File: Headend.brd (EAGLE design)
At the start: 65.4 x 48.6 mm, 56 parts, among them IC1 317EMP, Q1 12.288Mhz, SW1 SPST_TACT-KMR2, U1 TXS0102

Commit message: Update board design
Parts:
- moved R8 29.3 mm to (14.8, 17.8), turned to 180 degrees
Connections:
- removed net N$12: COMMS_CPU.GPIO15, R8.1
- removed net N$6: COMMS_CPU.RESET, R9.1, SW1.1, SW1.3
- new net TEENSYCS: COMMS_CPU.GPIO15, R8.2, UI_CPU.10
- new net WATCHDOG: COMMS_CPU.RESET, R9.1, SW1.1, SW1.3, UI_CPU.2
- net +3V3: no longer R8.2
- net GND: now also R8.1
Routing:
- net TEENSYCS: track 0.00 -> 46.7 mm
- net WATCHDOG: track 0.00 -> 39.3 mm
- net N$6: track 19.2 -> 0.00 mm
- net GND: track 55.6 -> 46.7 mm
- net XDCS: track 36.5 -> 45.0 mm
- net N$12: track 5.25 -> 0.00 mm
- net +3V3: track 172.4 -> 171.3 mm

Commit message: Update board with further tweaks
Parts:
- removed SW1: SPST_TACT-KMR2, adafruit:KMR2
- added C22, C23: 10uF, adafruit:C0402
- added PGM_SW: SPST_TACT-KMR2, adafruit:KMR2
- C1, C2: value 8uF -> 10uF
- C13, C14: value 33pF -> 10pF
- moved RESET_SW 37.3 mm to (17.8, 40.6), turned to 180 degrees
- moved R13 0.95 mm to (62.6, 17.4), turned to 315 degrees
- moved C7 0.32 mm to (51.7, 15.9)
- moved C10 0.32 mm to (49.6, 21.9)
- turned C6 to 315 degrees
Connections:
- net +3V3: now also C22.1, C23.1
- net GND: now also C22.2, C23.2, PGM_SW.2, PGM_SW.4; no longer SW1.2, SW1.4
- net WATCHDOG: now also RESET_SW.1, RESET_SW.3; no longer SW1.1, SW1.3
- net XDCS: now also PGM_SW.1, PGM_SW.3; no longer RESET_SW.1, RESET_SW.3
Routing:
- net GND: track 46.7 -> 28.7 mm
- net N$19: track 6.13 -> 4.63 mm

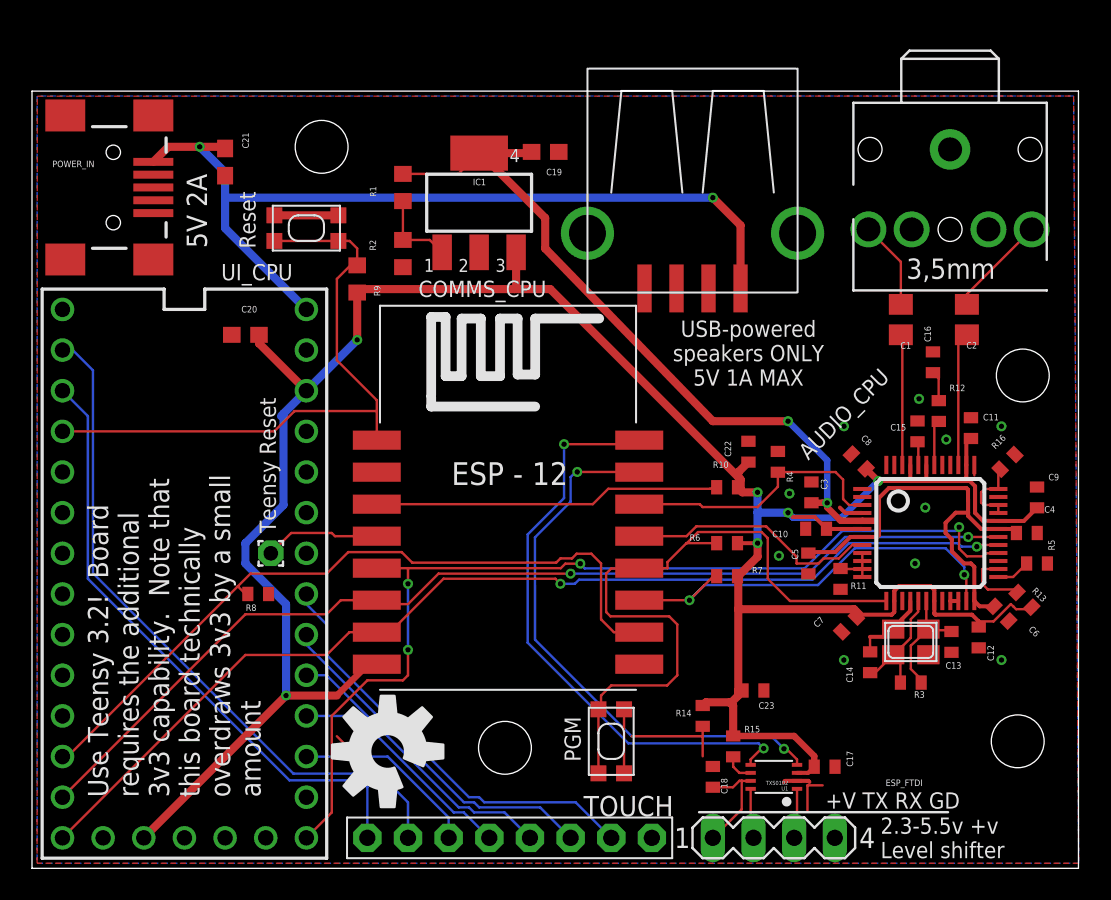
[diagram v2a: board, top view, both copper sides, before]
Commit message: Update design, clean up spurious resistor between 3v3 and Gnd, clean up some routing
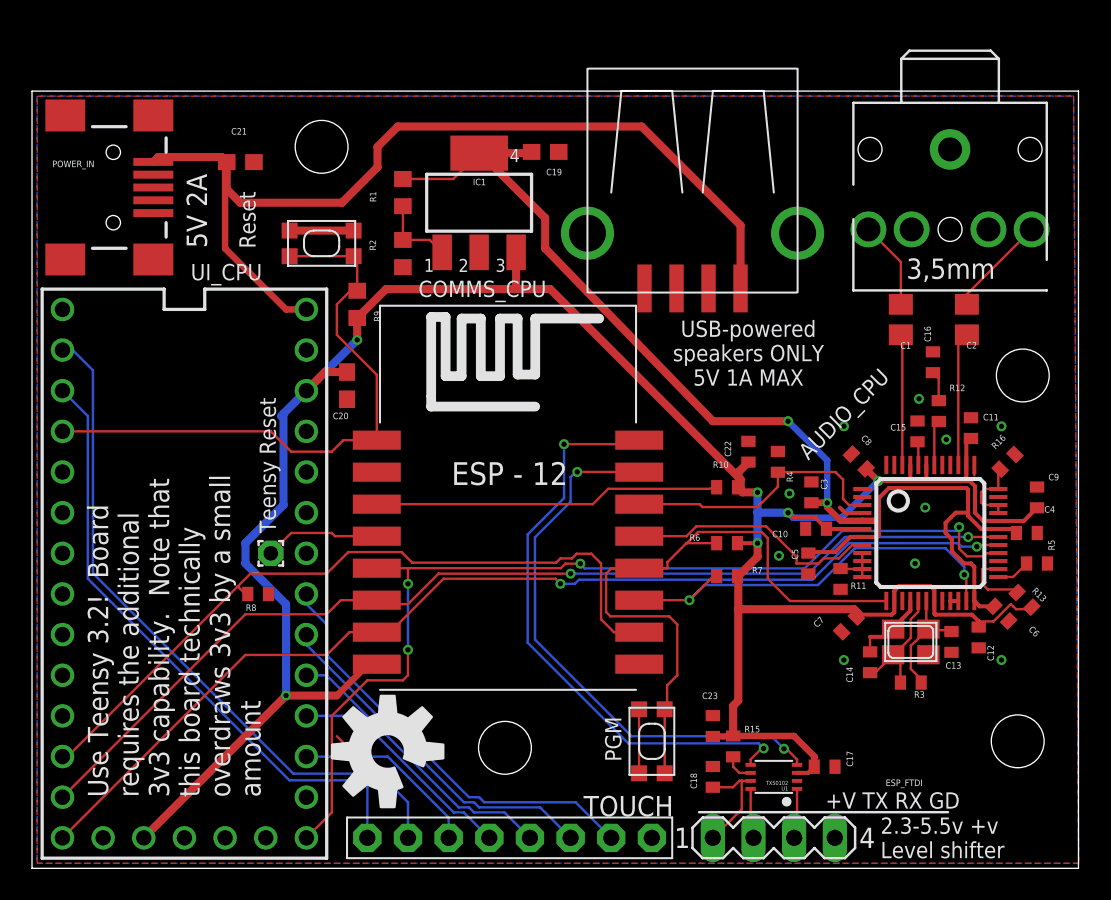
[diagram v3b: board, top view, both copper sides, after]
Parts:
- removed R14: 10k, adafruit:R0402
- moved C20 7.10 mm to (20.3, 30.8), turned to 270 degrees
- moved C23 3.38 mm to (43.2, 9.53), turned to 90 degrees
- moved PGM_SW 2.54 mm to (39.4, 8.57), turned to 270 degrees
- moved R9 1.59 mm to (21.0, 35.9)
- moved RESET_SW 1.35 mm to (18.7, 39.7)
- moved C21 0.95 mm to (13.7, 44.8), turned to 0 degrees
- moved R1 0.32 mm to (23.8, 42.9)
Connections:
- net +3V3: no longer R14.1
- net GND: no longer R14.2
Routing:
- net GND: track 28.7 -> 18.2 mm
- net +5V: track 54.7 -> 60.3 mm, vias 2 -> 0
- net XDCS: track 45.0 -> 41.2 mm
- net +3V3: track 170.9 -> 167.3 mm
- net WATCHDOG: track 39.3 -> 38.7 mm

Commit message: Updated with more reddit feedback
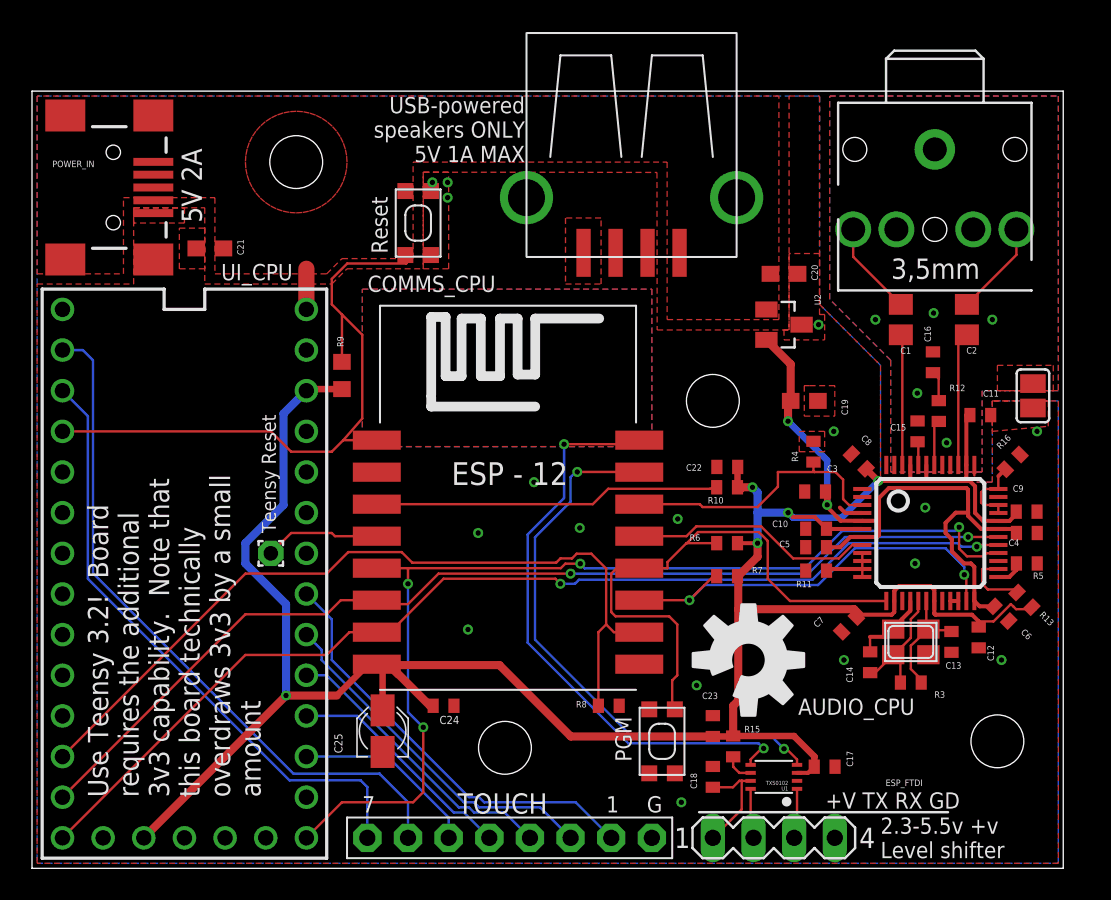
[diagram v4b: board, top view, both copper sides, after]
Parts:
- removed IC1: 317EMP, linear:SOT223
- removed R1: 240, adafruit:R0603
- removed R2: 106, adafruit:R0603
- added C24: 1uF, adafruit:C0402
- added C25: 4.7uF, adafruit:PANASONIC_A
- added SJ1: (no value), jumper:SJ
- added U2: AP7313, CustomParts:SOT23
- AUDIO_CPU: value VS1033 -> VS1063
- C20: value 0.1uF -> 1uF
- moved C20 28.2 mm to (47.6, 37.8), turned to 0 degrees
- moved LOGO1 23.3 mm to (45.4, 13.7), turned to 315 degrees
- moved R8 23.0 mm to (36.7, 10.8)
- moved C19 22.5 mm to (48.9, 29.8)
- moved STANDOFF2 19.4 mm to (43.2, 29.8)
- moved RESET_SW 6.16 mm to (24.8, 41.0), turned to 90 degrees
- moved C21 5.72 mm to (11.7, 39.4), turned to 180 degrees
- moved R9 4.55 mm to (20.0, 31.4)
- moved SPEAKER_PWR2 4.41 mm to (38.1, 42.5)
- moved R4 2.31 mm to (49.5, 26.7)
- moved STANDOFF4 1.85 mm to (17.1, 44.8)
- moved C22 1.63 mm to (44.1, 25.7), turned to 180 degrees
- moved R11 1.61 mm to (49.6, 19.2), turned to 180 degrees
- moved STANDOFF1 1.27 mm to (61.0, 8.57)
- moved C5 1.12 mm to (49.6, 20.7), turned to 180 degrees
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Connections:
- removed net N$5: IC1.1, R1.2, R2.1
- new net AGND: AUDIO_CPU.37, AUDIO_CPU.40, AUDIO_CPU.41, AUDIO_CPU.47, AUDIO_OUT.1, C15.2, C16.2, SJ1.2
- net +3V3: now also C24.1, C25.+; no longer C20.1, IC1.3
- net +5V: now also C20.1, U2.1
- net 1.8V: now also U2.2; no longer IC1.4, R1.1
- net GND: now also C24.2, C25.-, SJ1.1, U2.3; no longer AUDIO_CPU.37, AUDIO_CPU.40, AUDIO_CPU.41, AUDIO_CPU.47, AUDIO_OUT.1, C15.2, C16.2, R2.2
- net WATCHDOG: no longer RESET_SW.1
- net XDCS: no longer PGM_SW.1
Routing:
- net +5V: track 60.3 -> 2.54 mm
- net 1.8V: track 74.6 -> 42.7 mm
- net GND: track 18.2 -> 8.43 mm, vias 10 -> 17
- net +3V3: track 167.3 -> 159.8 mm, vias 6 -> 5
- net N$5: track 4.88 -> 0.00 mm
- net XDCS: track 41.2 -> 36.7 mm
- net TEENSYCS: track 46.7 -> 51.2 mm
- net SCLK: track 62.6 -> 64.7 mm
- net WATCHDOG: track 38.7 -> 40.6 mm
- net N$13: track 2.87 -> 3.75 mm
- net AGND: track 0.00 -> 0.67 mm, vias 0 -> 5
- net AUD_RESET: track 17.0 -> 17.7 mm
- net DREQ: track 15.9 -> 15.4 mm
- added copper zone on layer 1, net +5V
- added copper zone on layer 1, net AGND
- added copper zone on layer 16, net AGND
- added copper zone on layer 1, net N$5
- added copper zone on layer 16, net N$5
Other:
- board size 65.4 x 48.6 mm -> 64.4 x 48.6 mm
- board text added: "1"
- board text added: "7"
- board text added: "G"
